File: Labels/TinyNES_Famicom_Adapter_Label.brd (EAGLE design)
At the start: 70 x 10 mm, 0 parts

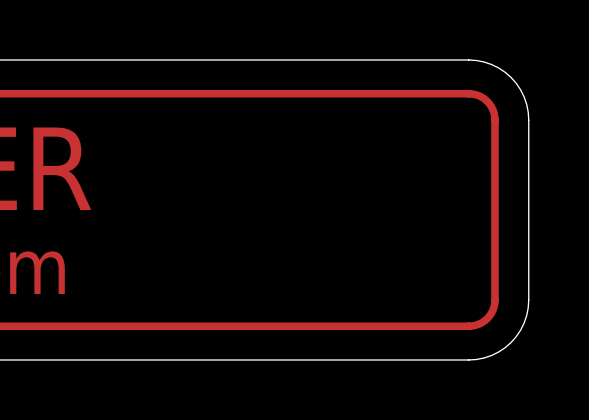
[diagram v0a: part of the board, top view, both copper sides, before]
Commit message: updated labels with new version
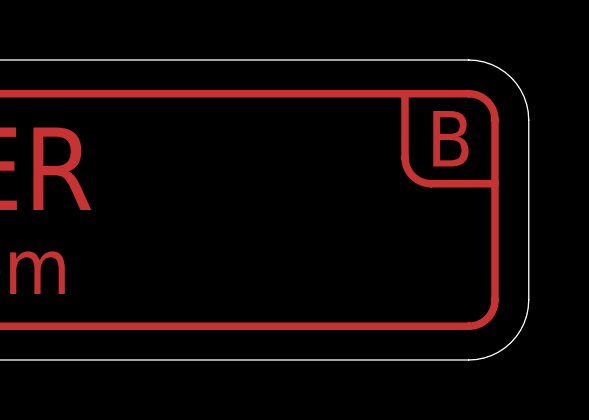
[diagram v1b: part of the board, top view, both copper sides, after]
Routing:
- net S$1: track 156.7 -> 162.2 mm
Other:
- board text added: "B"
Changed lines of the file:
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@@
 <text x="11" y="5" size="3.65" layer="1" ratio="10" align="center">TinyNES</text>
 <text x="22.375" y="3.125" size="1.85" layer="1" ratio="12" align="center-left">TD-TNES-FCA • tall-dog.com</text>
+<text x="67.375" y="7.375" size="1.85" layer="1" ratio="12" align="center">B</text>
 </plain>
 <attributes>
@@
 <wire x1="1.125" y1="2" x2="1.125" y2="8" width="0.25" layer="1"/>
 <wire x1="2" y1="1.125" x2="1.125" y2="2" width="0.25" layer="1" curve="-90"/>
+<wire x1="66.75" y1="5.875" x2="68.875" y2="5.875" width="0.25" layer="1"/>
+<wire x1="66.75" y1="5.875" x2="65.875" y2="6.75" width="0.25" layer="1" curve="-90"/>
+<wire x1="65.875" y1="8.875" x2="65.875" y2="6.75" width="0.25" layer="1"/>
 </signal>
 </signals>
